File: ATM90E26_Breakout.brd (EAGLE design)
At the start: 32.7 x 26.7 mm, 36 parts, among them J1 10p-2.54, Q1 8.192MHz, U1 ATM90E26

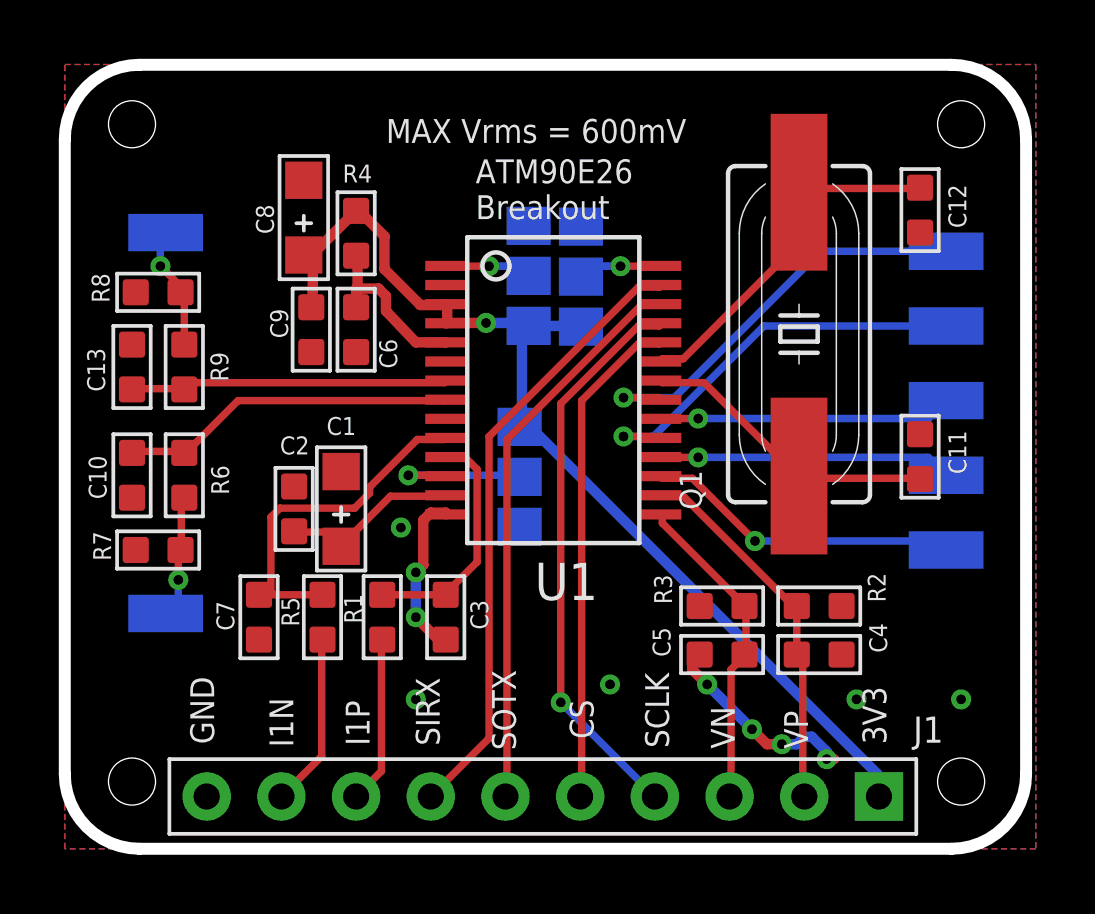
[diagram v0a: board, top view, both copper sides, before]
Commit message: Cosmetic changes to v1.0 ready for first fab
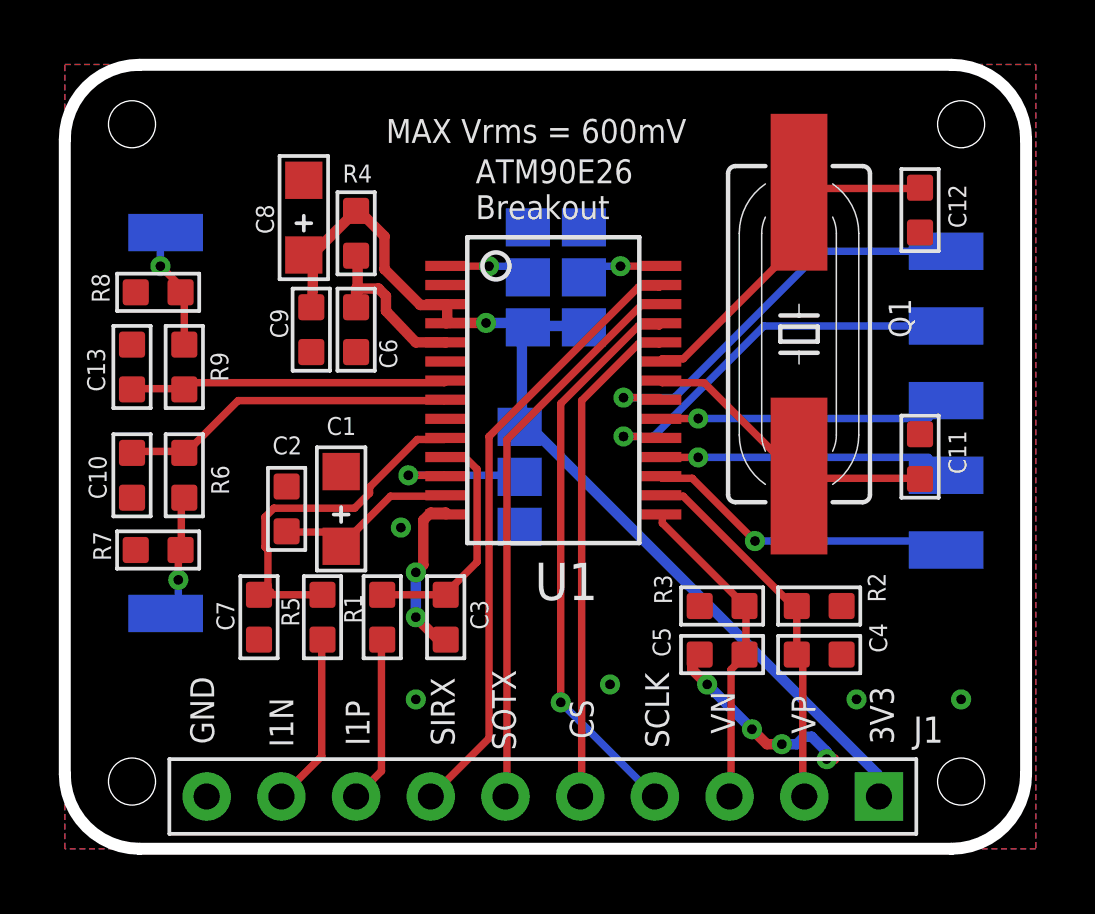
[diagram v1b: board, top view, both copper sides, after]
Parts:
- moved LOGO1 2.05 mm to (21.6, 8.84)
- moved C2 0.25 mm to (10.1, 11.6)
- moved MMD0 0.10 mm to (20.2, 19.4)
- moved MMD1 0.06 mm to (18.3, 19.4)
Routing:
- net I1N: track 12.3 -> 12.8 mm
